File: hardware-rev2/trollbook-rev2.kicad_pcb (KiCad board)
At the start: 2 copper layers, 160 x 120 mm, 7 parts, among them U1 MC68040FC33V, U2 EPF10K50VRC240, U4 HY57V561620, U5 HY57V561620, U6 IDT71V416, U7 TLC7524, U8 TLC7524

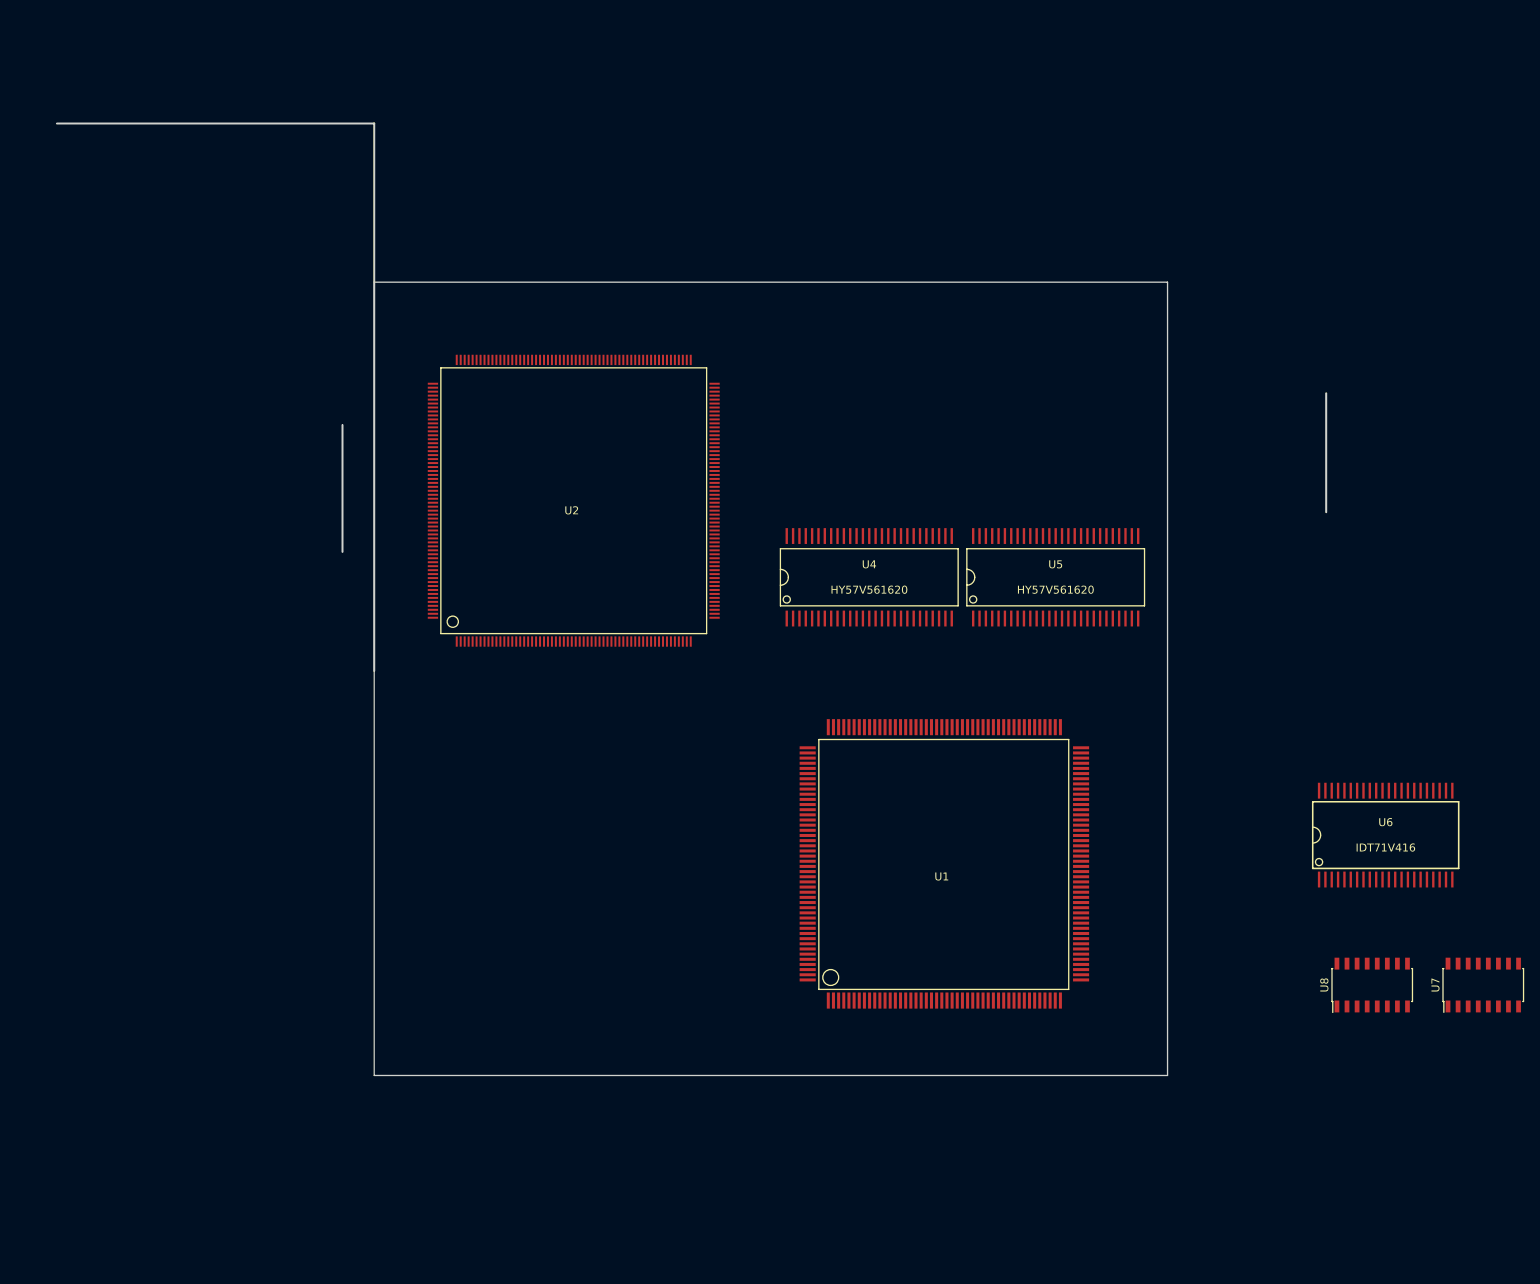
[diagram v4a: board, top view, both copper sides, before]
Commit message: started connecting processor to glue
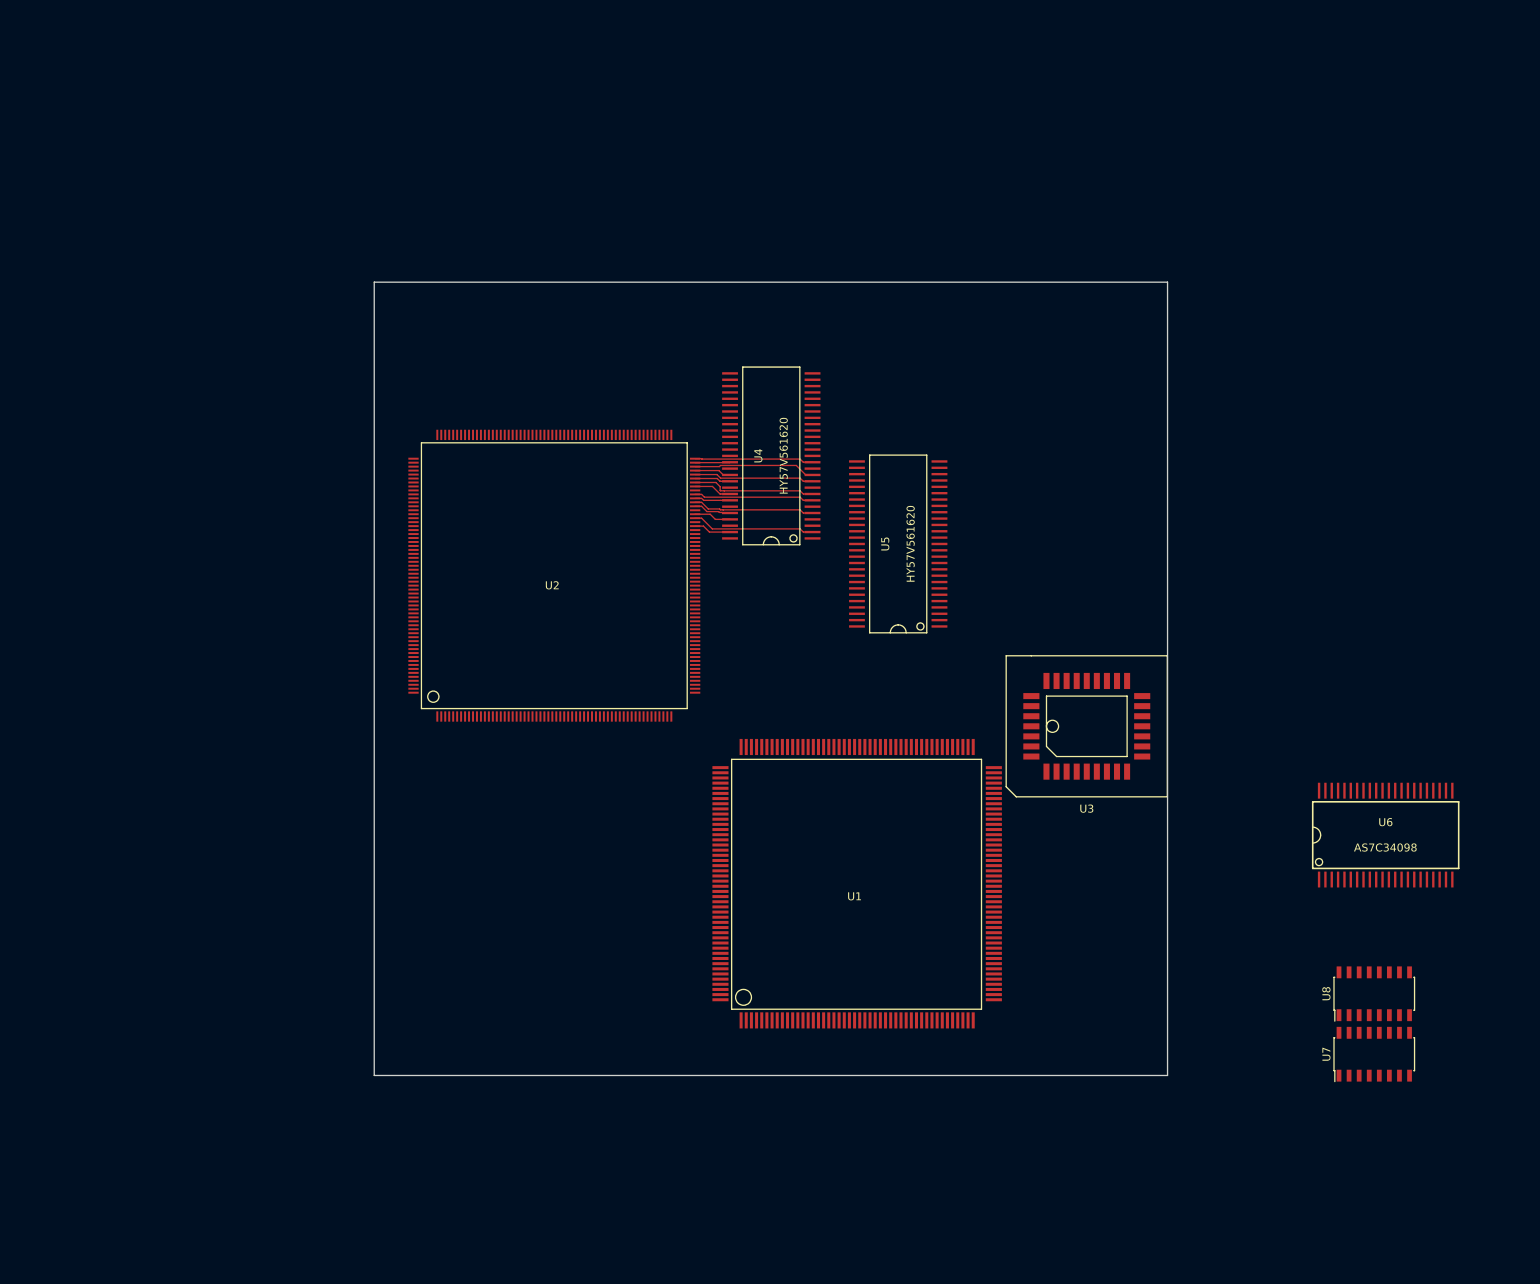
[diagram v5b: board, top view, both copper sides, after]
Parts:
- added U3: 39F040, SMD_Packages:PLCC-32, F.Cu at (189.8, 106.0)
- U6: value IDT71V416 -> AS7C34098
- moved U5 20.3 mm to (166.1, 83.0), turned to 90 degrees
- moved U4 19.7 mm to (150.1, 71.9), turned to 90 degrees
- moved U7 16.3 mm to (226.1, 147.3)
- moved U1 11.3 mm to (160.6, 126.2)
- moved U2 9.76 mm to (122.5, 87.2)
- moved U8 1.13 mm to (226.1, 139.7)
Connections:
- net Net-(U6-Pad29) renamed /LLD8
- net Net-(U6-Pad30) renamed /LLD9
- net Net-(U6-Pad31) renamed /LLD10
- net Net-(U6-Pad32) renamed /LLD11
- net Net-(U6-Pad35) renamed /LLD12
- net Net-(U6-Pad36) renamed /LLD13
- net Net-(U6-Pad37) renamed /LLD14
- net Net-(U6-Pad38) renamed /LLD15
- U1 pad 10: (no net) -> +3V3
- U1 pad 23: (no net) -> GND
- U1 pad 30: (no net) -> GND
- U2 pad 100: /A13 -> /D24
- U2 pad 101: /A14 -> /D23
- U2 pad 102: /A15 -> /D16
- U2 pad 103: /A16 -> /D15
- U2 pad 105: /A17 -> /D0
- U2 pad 106: /A18 -> /D14
- U2 pad 107: /A19 -> /D1
- U2 pad 108: /A20 -> /D13
- U2 pad 109: /A21 -> /D2
- U2 pad 110: /A22 -> /D12
- U2 pad 111: /A23 -> /D3
- U2 pad 113: /A24 -> /D11
- U2 pad 114: /A25 -> /D4
- U2 pad 115: /A26 -> /D10
- U2 pad 116: /A27 -> /D5
- U2 pad 117: /A28 -> /D9
- U2 pad 118: /A29 -> /D6
- U2 pad 119: /A30 -> /D8
- U2 pad 120: /A31 -> /D7
- U2 pad 39: /D0 -> /A10
- U2 pad 40: /D1 -> /A11
- U2 pad 41: /D2 -> /A12
- U2 pad 43: /D3 -> /A13
- U2 pad 44: /D4 -> /A14
- U2 pad 45: /D5 -> /A15
- U2 pad 46: /D6 -> /A16
- U2 pad 48: /D7 -> /A17
- U2 pad 49: /D8 -> /A18
- U2 pad 50: /D9 -> /A19
- U2 pad 51: /D10 -> /A20
- U2 pad 53: /D11 -> /A21
- U2 pad 54: /D12 -> /A22
- U2 pad 55: /D13 -> /A23
- U2 pad 56: /D14 -> /A24
- U2 pad 61: /D15 -> /A29
- U2 pad 62: /D16 -> /A30
- U2 pad 63: /D17 -> /A31
- U2 pad 64: /D18 -> /A28
- U2 pad 65: /D19 -> /A27
- U2 pad 66: /D20 -> /A26
- U2 pad 67: /D21 -> /A25
- U2 pad 68: /D22 -> /A9
- U2 pad 70: /D23 -> /A8
- U2 pad 71: /D24 -> /A7
- U2 pad 72: /D25 -> /A6
- U2 pad 73: /D26 -> /A5
- U2 pad 74: /D27 -> /A4
- U2 pad 75: /D28 -> /A3
- U2 pad 76: /D29 -> /A2
- U2 pad 78: /D30 -> /A1
- U2 pad 79: /D31 -> /A0
- U2 pad 80: /A0 -> /D31
- U2 pad 81: /A1 -> /D30
- U2 pad 82: /A2 -> /D17
- U2 pad 83: /A3 -> /D29
- U2 pad 84: /A4 -> /D18
- U2 pad 86: /A5 -> /D28
- U2 pad 87: /A6 -> /D19
- U2 pad 88: /A7 -> /D27
- U2 pad 94: /A8 -> /D20
- U2 pad 95: /A9 -> /D26
- U2 pad 97: /A10 -> /D21
- U2 pad 98: /A11 -> /D25
- U2 pad 99: /A12 -> /D22
- U4 pad 1: (no net) -> +3V3
- U4 pad 12: (no net) -> GND
- U4 pad 14: (no net) -> +3V3
- U4 pad 16: (no net) -> /RAMWE
- U4 pad 17: (no net) -> /RAMCAS
- U4 pad 18: (no net) -> /RAMRAS
- U4 pad 20: (no net) -> /RAMB0
- U4 pad 21: (no net) -> /RAMB1
- U4 pad 22: (no net) -> /RAMA10
- U4 pad 23: (no net) -> /RAMA0
- U4 pad 24: (no net) -> /RAMA1
- U4 pad 25: (no net) -> /RAMA2
- U4 pad 26: (no net) -> /RAMA3
- U4 pad 27: (no net) -> +3V3
- U4 pad 28: Net-(U4-Pad28) -> GND
- U4 pad 29: Net-(U4-Pad29) -> /RAMA4
- U4 pad 3: (no net) -> +3V3
- U4 pad 30: Net-(U4-Pad30) -> /RAMA5
- U4 pad 31: Net-(U4-Pad31) -> /RAMA6
- U4 pad 32: Net-(U4-Pad32) -> /RAMA7
- U4 pad 33: Net-(U4-Pad33) -> /RAMA8
- U4 pad 34: Net-(U4-Pad34) -> /RAMA9
- U4 pad 35: Net-(U4-Pad35) -> /RAMA11
- U4 pad 36: Net-(U4-Pad36) -> /RAMA12
- U4 pad 37: Net-(U4-Pad37) -> /RAMCKE
- U4 pad 38: Net-(U4-Pad38) -> /RAMCLK
- U4 pad 41: (no net) -> GND
- U4 pad 43: (no net) -> +3V3
- U4 pad 46: (no net) -> GND
- U4 pad 49: (no net) -> +3V3
- U4 pad 52: (no net) -> GND
- U4 pad 54: (no net) -> GND
- U4 pad 6: (no net) -> GND
- U4 pad 9: (no net) -> +3V3
- U5 pad 1: (no net) -> +3V3
- U5 pad 12: (no net) -> GND
- U5 pad 14: (no net) -> +3V3
- U5 pad 16: (no net) -> /RAMWE
- U5 pad 17: (no net) -> /RAMCAS
- U5 pad 18: (no net) -> /RAMRAS
- U5 pad 20: (no net) -> /RAMB0
- U5 pad 21: (no net) -> /RAMB1
- U5 pad 22: (no net) -> /RAMA10
- U5 pad 23: (no net) -> /RAMA0
- U5 pad 24: (no net) -> /RAMA1
- U5 pad 25: (no net) -> /RAMA2
- U5 pad 26: (no net) -> /RAMA3
- U5 pad 27: (no net) -> +3V3
- U5 pad 28: Net-(U5-Pad28) -> GND
- U5 pad 29: Net-(U5-Pad29) -> /RAMA4
- U5 pad 3: (no net) -> +3V3
- U5 pad 30: Net-(U5-Pad30) -> /RAMA5
- U5 pad 31: Net-(U5-Pad31) -> /RAMA6
- U5 pad 32: Net-(U5-Pad32) -> /RAMA7
- U5 pad 33: Net-(U5-Pad33) -> /RAMA8
- U5 pad 34: Net-(U5-Pad34) -> /RAMA9
- U5 pad 35: Net-(U5-Pad35) -> /RAMA11
- U5 pad 36: Net-(U5-Pad36) -> /RAMA12
- U5 pad 37: Net-(U5-Pad37) -> /RAMCKE
- U5 pad 38: Net-(U5-Pad38) -> /RAMCLK
- U5 pad 41: (no net) -> GND
- U5 pad 43: (no net) -> +3V3
- U5 pad 46: (no net) -> GND
- U5 pad 49: (no net) -> +3V3
- U5 pad 52: (no net) -> GND
- U5 pad 54: (no net) -> GND
- U5 pad 6: (no net) -> GND
- U5 pad 9: (no net) -> +3V3
- U6 pad 11: (no net) -> +3V3
- U6 pad 12: (no net) -> GND
- U6 pad 33: Net-(U6-Pad33) -> +3V3
- U6 pad 34: Net-(U6-Pad34) -> GND
- U7 pad 10: (no net) -> /ROMD1
- U7 pad 11: (no net) -> /ROMD0
- U7 pad 13: (no net) -> /DACWR
- U7 pad 4: (no net) -> /ROMD7
- U7 pad 5: (no net) -> /ROMD6
- U7 pad 6: (no net) -> /ROMD5
- U7 pad 7: (no net) -> /ROMD4
- U7 pad 8: (no net) -> /ROMD3
- U7 pad 9: (no net) -> /ROMD2
- U8 pad 10: (no net) -> /ROMD1
- U8 pad 11: (no net) -> /ROMD0
- U8 pad 13: (no net) -> /DACWR
- U8 pad 4: (no net) -> /ROMD7
- U8 pad 5: (no net) -> /ROMD6
- U8 pad 6: (no net) -> /ROMD5
- U8 pad 7: (no net) -> /ROMD4
- U8 pad 8: (no net) -> /ROMD3
- U8 pad 9: (no net) -> /ROMD2
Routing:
- net (no net): track 140.0 -> 0.00 mm
- net /D4: track 0.00 -> 15.7 mm
- net /D0: track 0.00 -> 15.5 mm
- net /D2: track 0.00 -> 15.4 mm
- net /D6: track 0.00 -> 15.4 mm
- net /D5: track 0.00 -> 15.2 mm
- net /D3: track 0.00 -> 15.1 mm
- net /D7: track 0.00 -> 15.0 mm
- net /D11: track 0.00 -> 4.79 mm
- net /D13: track 0.00 -> 4.75 mm
- net /D15: track 0.00 -> 4.71 mm
- net /D14: track 0.00 -> 4.67 mm
- net /D9: track 0.00 -> 4.63 mm
- net /D10: track 0.00 -> 4.54 mm
- net /D12: track 0.00 -> 4.50 mm
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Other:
- board size 160 x 120 mm -> 100 x 100 mm
- net class Default: clearance 0.2032 -> 0.1651; trace_width 0.2032 -> 0.1651
- rule trace_clearance: 0.2032 -> 0.1651
- rule trace_min: 0.2 -> 0.127

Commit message: added oscillator lib
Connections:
- U2 pad 100: /D24 -> /D22
- U2 pad 101: /D23 -> /D24
- U2 pad 102: /D16 -> /D23
- U2 pad 80: /D31 -> /D16
- U2 pad 81: /D30 -> /D31
- U2 pad 82: /D17 -> /D30
- U2 pad 83: /D29 -> /D17
- U2 pad 84: /D18 -> /D29
- U2 pad 86: /D28 -> /D18
- U2 pad 87: /D19 -> /D28
- U2 pad 88: /D27 -> /D19
- U2 pad 94: /D20 -> /D27
- U2 pad 95: /D26 -> /D20
- U2 pad 97: /D21 -> /D26
- U2 pad 98: /D25 -> /D21
- U2 pad 99: /D22 -> /D25
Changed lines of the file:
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@@
-(kicad_pcb (version 4) (host pcbnew 0.201509071501+6164~29~ubuntu14.04.1-product)
+(kicad_pcb (version 4) (host pcbnew "(2015-08-21 BZR 6112)-product")
   (general
     (links 324)
     (no_connects 277)
-    (area 99.924999 49.924999 236.965101 151.210101)
+    (area 99.924999 49.924999 200.075001 150.075001)
     (thickness 1.6)
     (drawings 4)
@@
       (net 3 /A1))
     (pad 80 smd rect (at 18 5 90) (size 0.25 1.3) (layers F.Cu F.Paste F.Mask)
+      (net 53 /D16))
+    (pad 81 smd rect (at 18 4.5 90) (size 0.25 1.3) (layers F.Cu F.Paste F.Mask)
       (net 39 /D31))
-    (pad 81 smd rect (at 18 4.5 90) (size 0.25 1.3) (layers F.Cu F.Paste F.Mask)
+    (pad 82 smd rect (at 18 4 90) (size 0.25 1.3) (layers F.Cu F.Paste F.Mask)
       (net 35 /D30))
-    (pad 82 smd rect (at 18 4 90) (size 0.25 1.3) (layers F.Cu F.Paste F.Mask)
+    (pad 83 smd rect (at 18 3.5 90) (size 0.25 1.3) (layers F.Cu F.Paste F.Mask)
       (net 51 /D17))
-    (pad 83 smd rect (at 18 3.5 90) (size 0.25 1.3) (layers F.Cu F.Paste F.Mask)
+    (pad 84 smd rect (at 18 3 90) (size 0.25 1.3) (layers F.Cu F.Paste F.Mask)
       (net 36 /D29))
-    (pad 84 smd rect (at 18 3 90) (size 0.25 1.3) (layers F.Cu F.Paste F.Mask)
+    (pad 85 smd rect (at 18 2.5 90) (size 0.25 1.3) (layers F.Cu F.Paste F.Mask)
+      (net 1 GND))
+    (pad 86 smd rect (at 18 2 90) (size 0.25 1.3) (layers F.Cu F.Paste F.Mask)
       (net 62 /D18))
-    (pad 85 smd rect (at 18 2.5 90) (size 0.25 1.3) (layers F.Cu F.Paste F.Mask)
-      (net 1 GND))
-    (pad 86 smd rect (at 18 2 90) (size 0.25 1.3) (layers F.Cu F.Paste F.Mask)
+    (pad 87 smd rect (at 18 1.5 90) (size 0.25 1.3) (layers F.Cu F.Paste F.Mask)
       (net 37 /D28))
-    (pad 87 smd rect (at 18 1.5 90) (size 0.25 1.3) (layers F.Cu F.Paste F.Mask)
+    (pad 88 smd rect (at 18 1 90) (size 0.25 1.3) (layers F.Cu F.Paste F.Mask)
       (net 60 /D19))
-    (pad 88 smd rect (at 18 1 90) (size 0.25 1.3) (layers F.Cu F.Paste F.Mask)
-      (net 38 /D27))
     (pad 89 smd rect (at 18 0.5 90) (size 0.25 1.3) (layers F.Cu F.Paste F.Mask)
       (net 2 +3V3))
@@
       (net 45 /D10))
     (pad 94 smd rect (at 18 -2 90) (size 0.25 1.3) (layers F.Cu F.Paste F.Mask)
-      (net 61 /D20))
+      (net 38 /D27))
     (pad 91 smd rect (at 18 -0.5 90) (size 0.25 1.3) (layers F.Cu F.Paste F.Mask))
     (pad 92 smd rect (at 18 -1 90) (size 0.25 1.3) (layers F.Cu F.Paste F.Mask))
@@
       (net 1 GND))
     (pad 95 smd rect (at 18 -2.5 90) (size 0.25 1.3) (layers F.Cu F.Paste F.Mask)
+      (net 61 /D20))
+    (pad 99 smd rect (at 18 -4.5 90) (size 0.25 1.3) (layers F.Cu F.Paste F.Mask)
+      (net 56 /D25))
+    (pad 96 smd rect (at 18 -3 90) (size 0.25 1.3) (layers F.Cu F.Paste F.Mask)
+      (net 2 +3V3))
+    (pad 97 smd rect (at 18 -3.5 90) (size 0.25 1.3) (layers F.Cu F.Paste F.Mask)
       (net 54 /D26))
-    (pad 99 smd rect (at 18 -4.5 90) (size 0.25 1.3) (layers F.Cu F.Paste F.Mask)
+    (pad 98 smd rect (at 18 -4 90) (size 0.25 1.3) (layers F.Cu F.Paste F.Mask)
+      (net 59 /D21))
+    (pad 100 smd rect (at 18 -5 90) (size 0.25 1.3) (layers F.Cu F.Paste F.Mask)
       (net 58 /D22))
-    (pad 96 smd rect (at 18 -3 90) (size 0.25 1.3) (layers F.Cu F.Paste F.Mask)
-      (net 2 +3V3))
-    (pad 97 smd rect (at 18 -3.5 90) (size 0.25 1.3) (layers F.Cu F.Paste F.Mask)
-      (net 59 /D21))
-    (pad 98 smd rect (at 18 -4 90) (size 0.25 1.3) (layers F.Cu F.Paste F.Mask)
-      (net 56 /D25))
-    (pad 100 smd rect (at 18 -5 90) (size 0.25 1.3) (layers F.Cu F.Paste F.Mask)
+    (pad 104 smd rect (at 18 -7 90) (size 0.25 1.3) (layers F.Cu F.Paste F.Mask)
+      (net 1 GND))
+    (pad 101 smd rect (at 18 -5.5 90) (size 0.25 1.3) (layers F.Cu F.Paste F.Mask)
       (net 55 /D24))
-    (pad 104 smd rect (at 18 -7 90) (size 0.25 1.3) (layers F.Cu F.Paste F.Mask)
-      (net 1 GND))
-    (pad 101 smd rect (at 18 -5.5 90) (size 0.25 1.3) (layers F.Cu F.Paste F.Mask)
+    (pad 102 smd rect (at 18 -6 90) (size 0.25 1.3) (layers F.Cu F.Paste F.Mask)
       (net 57 /D23))
-    (pad 102 smd rect (at 18 -6 90) (size 0.25 1.3) (layers F.Cu F.Paste F.Mask)
-      (net 53 /D16))
     (pad 103 smd rect (at 18 -6.5 90) (size 0.25 1.3) (layers F.Cu F.Paste F.Mask)
       (net 52 /D15))
